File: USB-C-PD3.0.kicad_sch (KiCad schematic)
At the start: 62 parts, among them J10 PD_I2C, J9 USB_C_PD, U10 BQ25756RRVT, U12 TPS76333, U3 TVS2200DRV, U4 CAT24C512WI-GT3, U7 TPS25751DREFR, U8 LMR51450

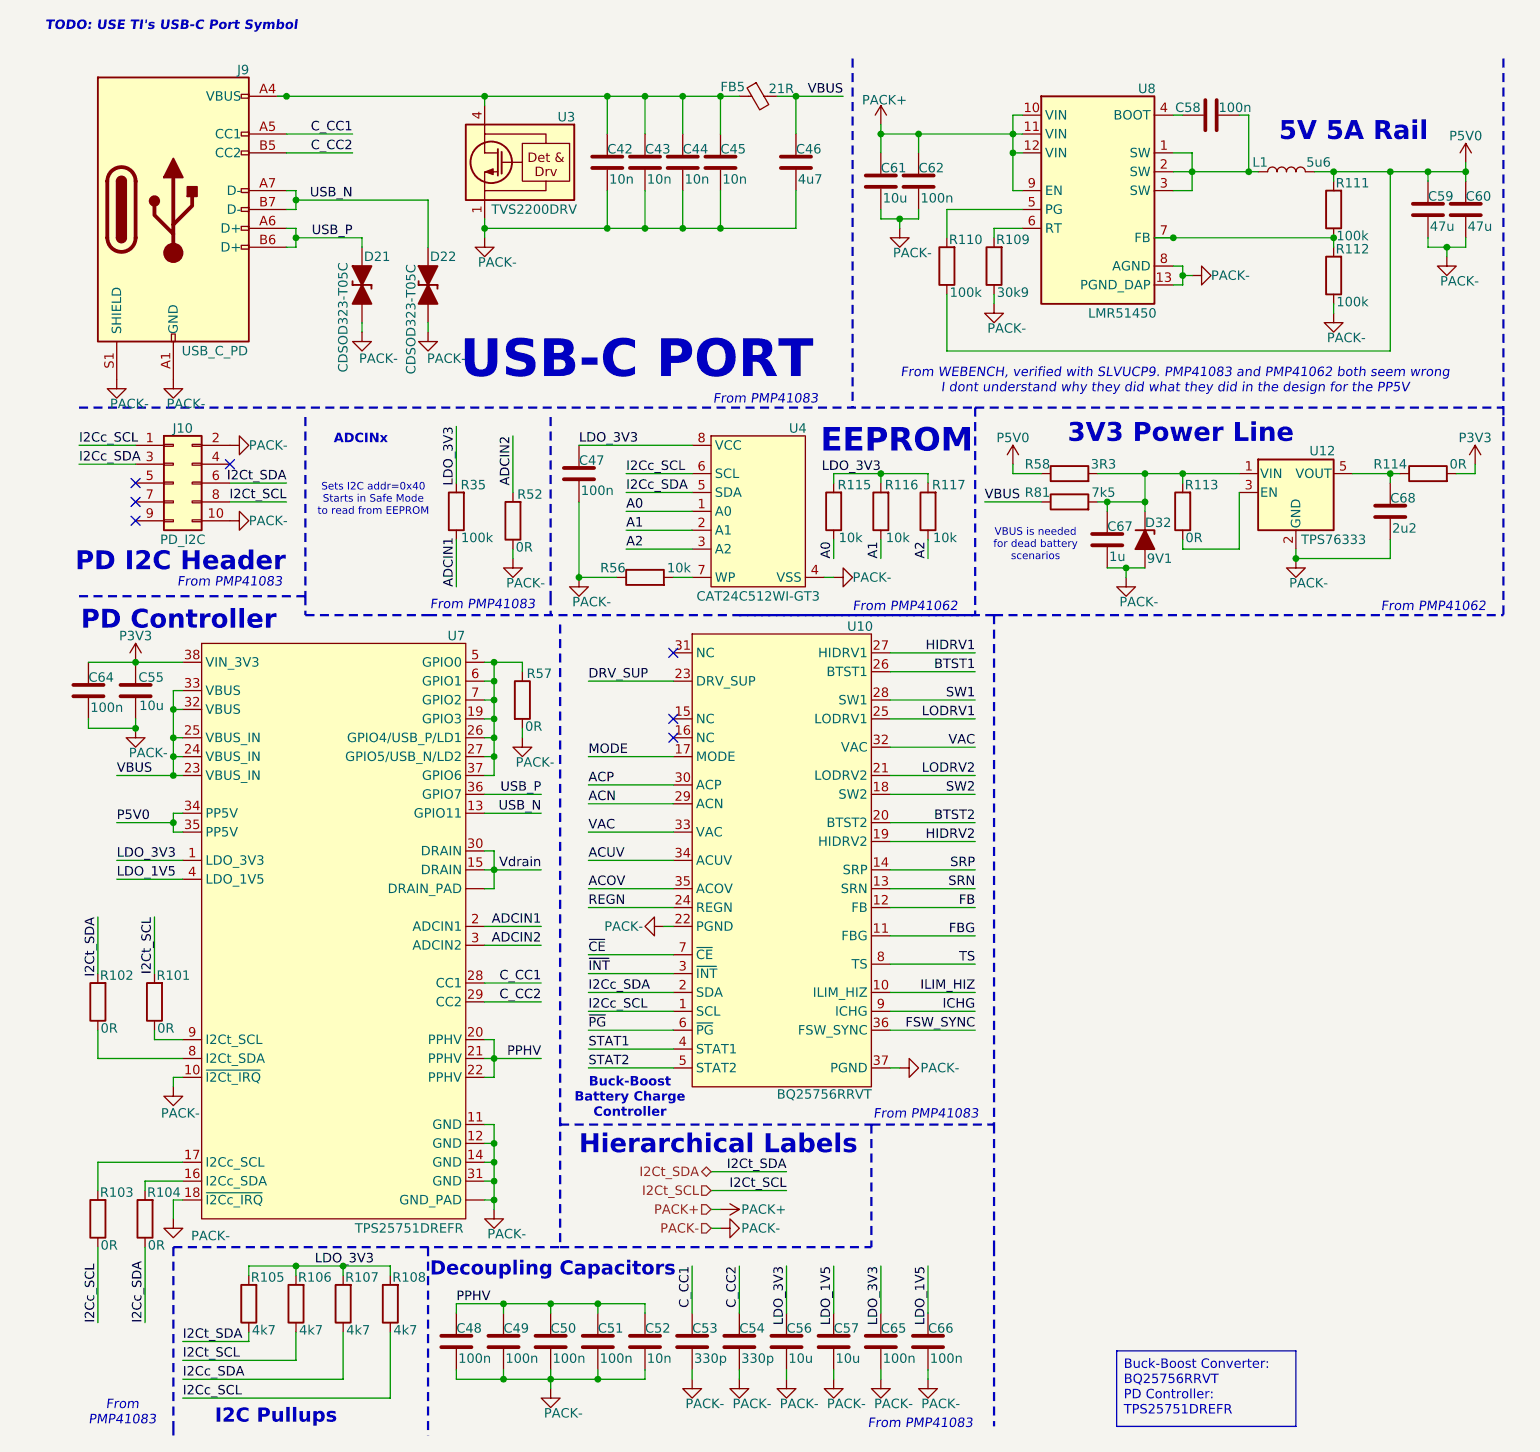
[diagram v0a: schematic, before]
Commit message: Restructured Layout
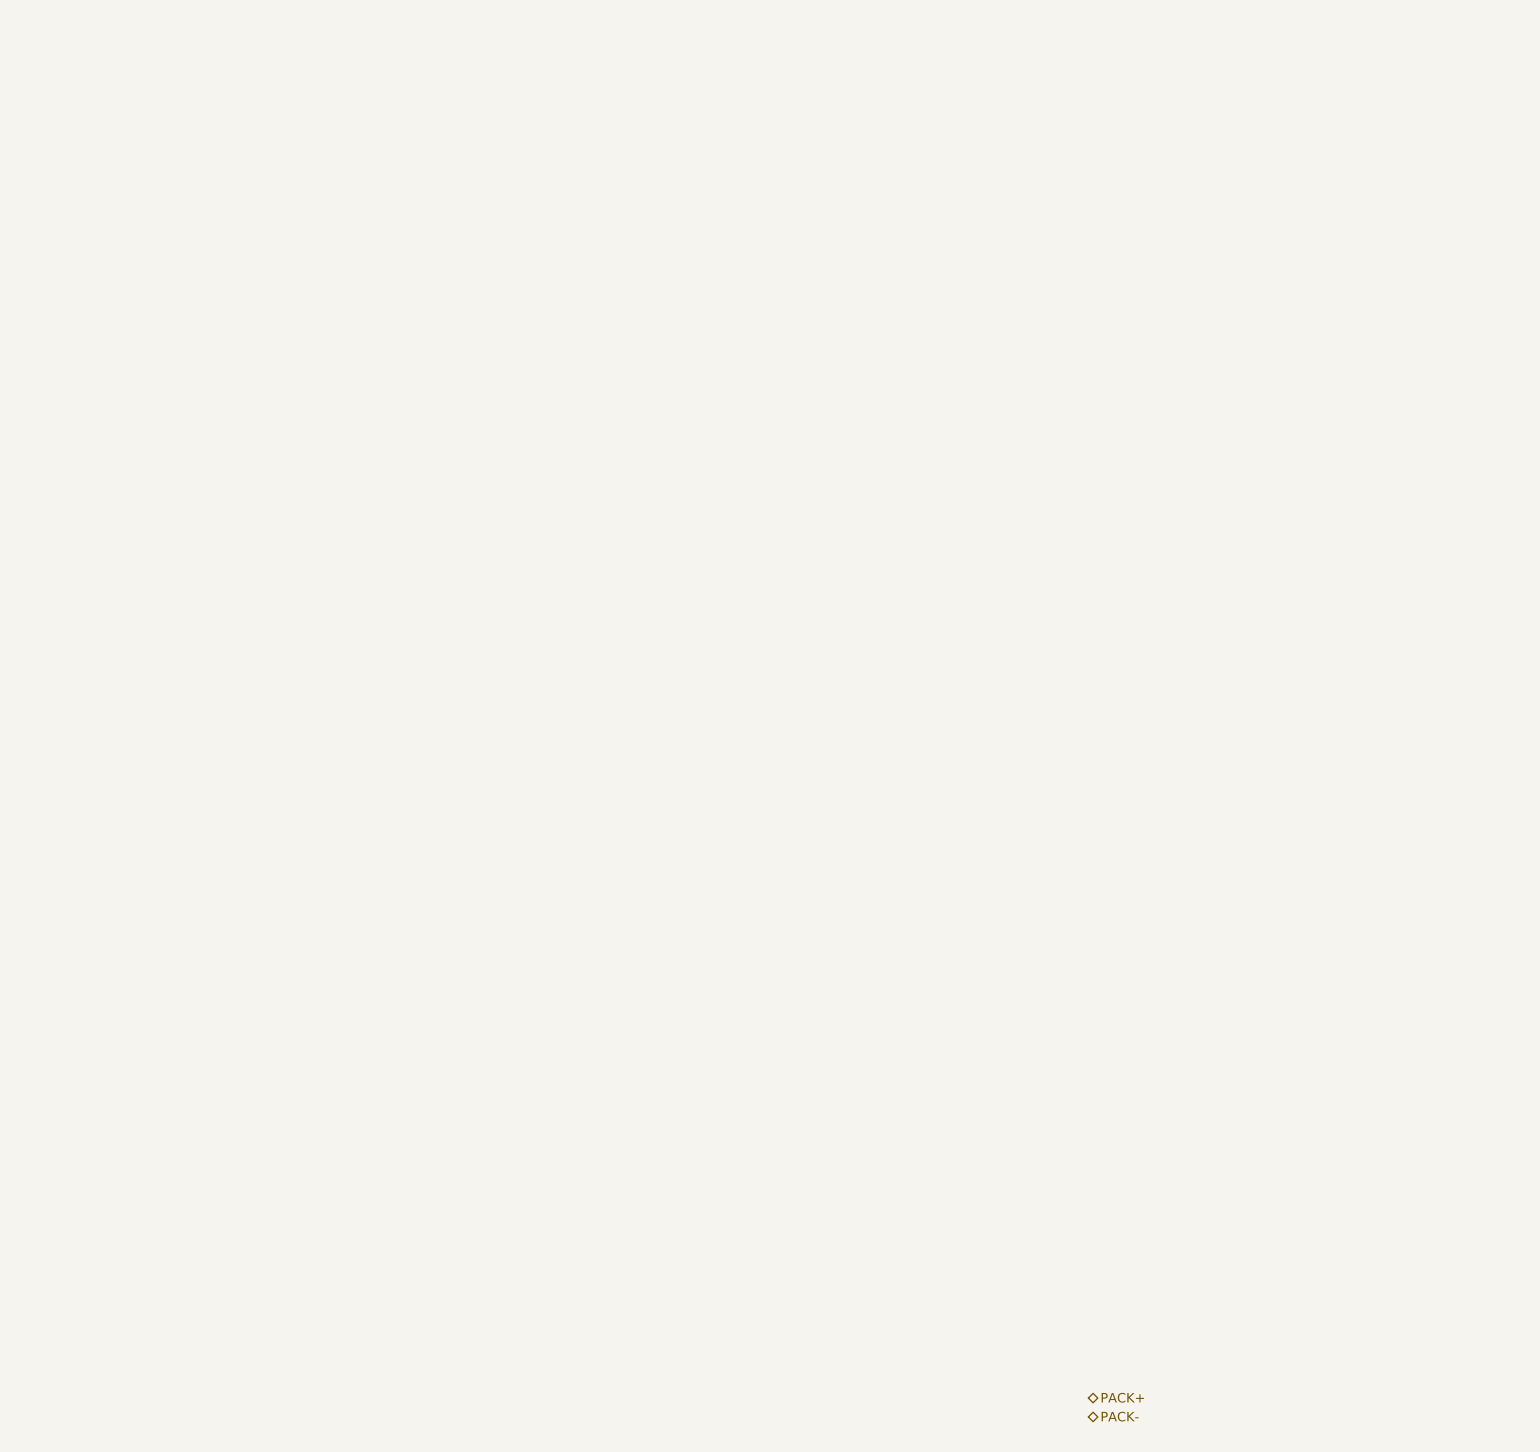
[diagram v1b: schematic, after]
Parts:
- removed C42, C43, C44, C45, C52: 10n, symbol Device:C
- removed C46: 4u7, symbol Device:C
- removed C47, C48, C49, C50, C51, C58, C62, C64, C65, C66: 100n, symbol Device:C
- removed C53, C54: 330p, symbol Device:C
- removed C55, C56, C57, C61: 10u, symbol Device:C
- removed C59, C60: 47u, symbol Device:C
- removed C67: 1u, symbol Device:C
- removed C68: 2u2, symbol Device:C
- removed D21, D22: CDSOD323-T05C, PCM_Diode_SMD_AKL:D_SOD-323F_TVS, symbol PCM_Diode_TVS_AKL:CDSOD323-T05C
- removed D32: 9V1, symbol Device:D_Zener_Filled
- removed FB5: 21R, symbol Device:FerriteBead_Small
- removed J10: PD_I2C, symbol Connector_Generic:Conn_02x05_Odd_Even
- removed J9: USB_C_PD, symbol Connector:USB_C_Receptacle_USB2.0_14P
- removed L1: 5u6, symbol Device:L
- removed R101, R102, R103, R104, R113, R114, R52, R57: 0R, symbol Device:R
- removed R105, R106, R107, R108: 4k7, symbol Device:R
- removed R109: 30k9, symbol Device:R
- removed R110, R111, R112, R35: 100k, symbol Device:R
- removed R115, R116, R117, R56: 10k, symbol Device:R
- removed R58: 3R3, symbol Device:R
- removed R81: 7k5, symbol Device:R
- removed U10: BQ25756RRVT, symbol Battery_Management:BQ25756RRVT
- removed U12: TPS76333, Package_TO_SOT_SMD:SOT-23-5, symbol Regulator_Linear:TPS76333
- removed U3: TVS2200DRV, Package_SON:WSON-6-1EP_2x2mm_P0.65mm_EP1x1.6mm, symbol Power_Protection:TVS2200DRV
- removed U4: CAT24C512WI-GT3, symbol Memory_EEPROM:CAT24C512WI-GT3
- removed U7: TPS25751DREFR, symbol Interface_USB:TPS25751DREFR
- removed U8: LMR51450, Package_SON:WSON-12-1EP_3x3mm_P0.5mm_EP1.5x2.5mm, symbol Regulator_Switching:LMR51450
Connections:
- no-connect marks 7 -> 0
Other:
- note removed: "3V3 Power Line"
- note removed: "5V 5A Rail"
- note removed: "ADCINx"
- note removed: "Buck-Boost Battery Charge Controller"
- note removed: "Decoupling Capacitors"
- note removed: "EEPROM"
- note removed: "From PMP41062"
- note removed: "From PMP41083"
- note removed: "From WEBENCH, verified with SLVUCP9. PMP41083 and PMP41062 both seem wrong I dont understand why they did what they did in the design for the PP5V"
- note removed: "Hierarchical Labels"
- note removed: "I2C Pullups"
- note removed: "PD Controller"
- note removed: "PD I2C Header"
- note removed: "Sets I2C addr=0x40 Starts in Safe Mode to read from EEPROM"
- note removed: "TODO: USE TI's USB-C Port Symbol"
- note removed: "USB-C PORT"
- note removed: "VBUS is needed for dead battery scenarios"
